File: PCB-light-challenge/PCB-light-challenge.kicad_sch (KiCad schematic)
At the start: 1 part

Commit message: Library toegevoegd
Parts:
- added U-PICO2: ~, symbol Light_challenge:Raspeberry_Pico
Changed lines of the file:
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@@
 (kicad_sch (version 20230121) (generator eeschema)
   (paper "A4")
+  (symbol (lib_id "Light_challenge:Raspeberry_Pico") (at 72.39 81.28 0) (unit 1)
+    (in_bom yes) (on_board yes) (dnp no) (fields_autoplaced)
+    (property "Reference" "U-PICO2" (at 87.63 79.0481 0)
+      (effects (font (size 1.27 1.27)))
+    )
+    (property "Value" "~" (at 72.39 81.28 0)
+      (effects (font (size 1.27 1.27)))
+    )
+    (property "Footprint" "" (at 72.39 81.28 0)
+      (effects (font (size 1.27 1.27)) hide)
+    )
+    (property "Datasheet" "" (at 72.39 81.28 0)
+      (effects (font (size 1.27 1.27)) hide)
+    )
+    (pin "")
+    (pin "")
+    (pin "")
+    (pin "")
+    (pin "")
+    (pin "")
+    (pin "")
+    (pin "")
+    (pin "")
+    (pin "")
+    (pin "")
+    (pin "")
+    (pin "")
+    (pin "")
+    (pin "")
+    (pin "")
+    (pin "")
+    (pin "")
+    (pin "")
+    (pin "")
+    (pin "")
+    (pin "")
+    (pin "")
+    (pin "")
+    (pin "")
+    (pin "")
+    (pin "")
+    (pin "")
+    (pin "")
+    (pin "")
+    (pin "")
+    (pin "")
+    (pin "")
+    (pin "")
+    (pin "")
+    (pin "")
+    (pin "")
+    (pin "")
+    (pin "")
+    (pin "")
+    (pin "")
+    (pin "")
+    (pin "")
+    (instances
+      (project "PCB-light-challenge"
+        (path "/35573e8f-7834-430c-81d2-239f316c7834"
+          (reference "U-PICO2") (unit 1)
+        )
+      )
+    )
+  )
   (symbol (lib_id "Light_challenge:Raspeberry_Pico") (at 127 81.28 0) (unit 1)
     (in_bom yes) (on_board yes) (dnp no) (fields_autoplaced)
-    (property "Reference" "U-PICO1" (at 142.24 77.47 0)
+    (property "Reference" "U-PICO1" (at 142.24 77.47 0) (show_name)
       (effects (font (size 1.27 1.27)))
     )
-    (property "Value" "~" (at 127 81.28 0)
+    (property "Value" "~" (at 127 81.28 0) (show_name)
       (effects (font (size 1.27 1.27)))
     )

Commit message: Opnieuw
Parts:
- removed U-PICO1: ~, symbol Light_challenge:Raspeberry_Pico
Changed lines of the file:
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@@
-    )
-  )
-  (symbol (lib_id "Light_challenge:Raspeberry_Pico") (at 127 81.28 0) (unit 1)
-    (in_bom yes) (on_board yes) (dnp no) (fields_autoplaced)
-    (property "Reference" "U-PICO1" (at 142.24 77.47 0) (show_name)
-      (effects (font (size 1.27 1.27)))
-    )
-    (property "Value" "~" (at 127 81.28 0) (show_name)
-      (effects (font (size 1.27 1.27)))
-    )
-    (property "Footprint" "" (at 127 81.28 0)
-      (effects (font (size 1.27 1.27)) hide)
-    )
-    (property "Datasheet" "" (at 127 81.28 0)
-      (effects (font (size 1.27 1.27)) hide)
-    )
-    (pin "")
-    (pin "")
-    (pin "")
-    (pin "")
-    (pin "")
-    (pin "")
-    (pin "")
-    (pin "")
-    (pin "")
-    (pin "")
-    (pin "")
-    (pin "")
-    (pin "")
-    (pin "")
-    (pin "")
-    (pin "")
-    (pin "")
-    (pin "")
-    (pin "")
-    (pin "")
-    (pin "")
-    (pin "")
-    (pin "")
-    (pin "")
-    (pin "")
-    (pin "")
-    (pin "")
-    (pin "")
-    (pin "")
-    (pin "")
-    (pin "")
-    (pin "")
-    (pin "")
-    (pin "")
-    (pin "")
-    (pin "")
-    (pin "")
-    (pin "")
-    (pin "")
-    (pin "")
-    (pin "")
-    (pin "")
-    (pin "")
-    (instances
-      (project "PCB-light-challenge"
-        (path "/35573e8f-7834-430c-81d2-239f316c7834"
-          (reference "U-PICO1") (unit 1)
-        )
-      )
     )
   )

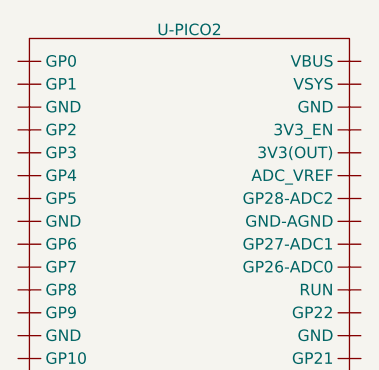
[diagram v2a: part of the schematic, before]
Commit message: pico footprint
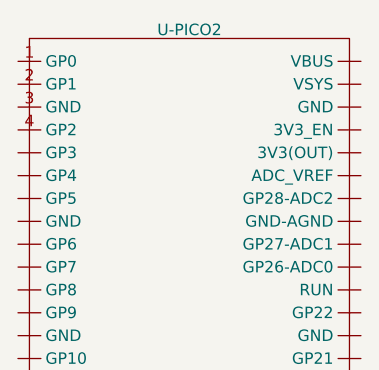
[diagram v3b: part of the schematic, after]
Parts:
- U-PICO2: footprint (none) -> custom_footprint_pico:Pico_light challenge
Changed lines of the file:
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@@
       (effects (font (size 1.27 1.27)))
     )
-    (property "Footprint" "" (at 72.39 81.28 0)
+    (property "Footprint" "custom_footprint_pico:Pico_light challenge" (at 72.39 81.28 0)
       (effects (font (size 1.27 1.27)) hide)
     )
@@
     (pin "")
     (pin "")
-    (pin "")
-    (pin "")
-    (pin "")
-    (pin "")
+    (pin "1")
+    (pin "2")
+    (pin "3")
+    (pin "4")
     (instances
       (project "PCB-light-challenge"

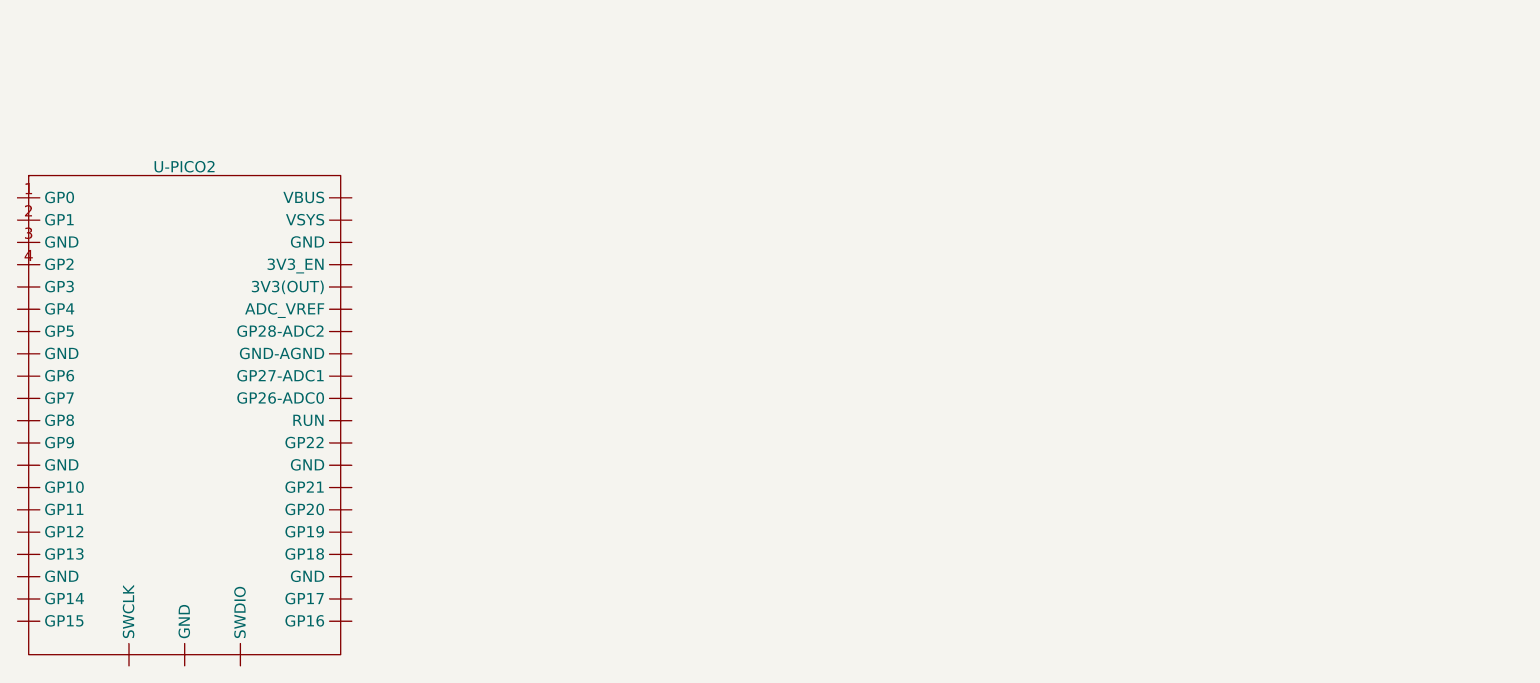
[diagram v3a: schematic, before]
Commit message: Hierarchische blad toegevoegd voor de microcontroller en battery charger
Dit moet gedaan worden voor elke deel van het totale circuit. Dit maakt de file beter leesbaar
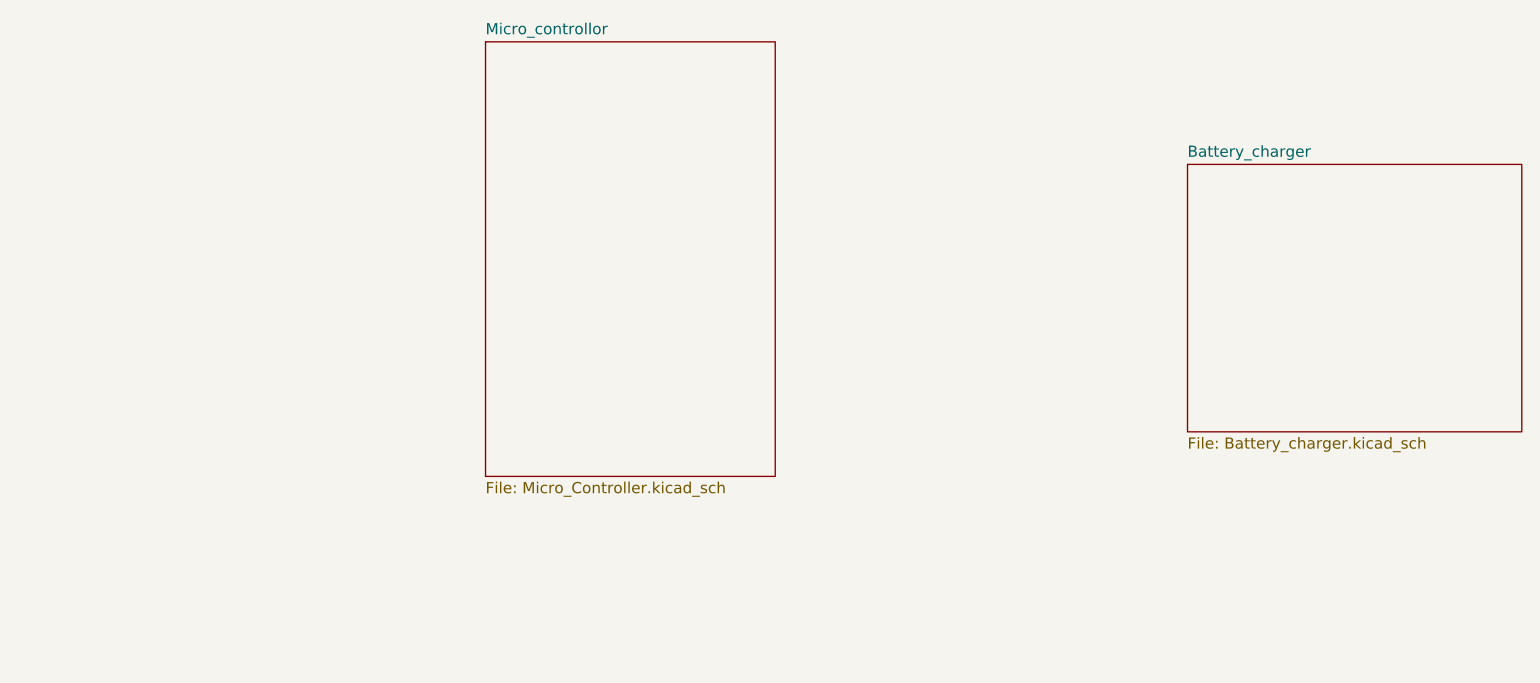
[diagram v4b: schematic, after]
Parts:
- removed U-PICO2: ~, custom_footprint_pico:Pico_light challenge, symbol Light_challenge:Raspeberry_Pico
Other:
- added sheet Battery_charger (Battery_charger.kicad_sch)
- added sheet Micro_controllor (Micro_Controller.kicad_sch)
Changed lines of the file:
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@@
 (kicad_sch (version 20230121) (generator eeschema)
   (paper "A4")
-  (symbol (lib_id "Light_challenge:Raspeberry_Pico") (at 72.39 81.28 0) (unit 1)
-    (in_bom yes) (on_board yes) (dnp no) (fields_autoplaced)
-    (property "Reference" "U-PICO2" (at 87.63 79.0481 0)
-      (effects (font (size 1.27 1.27)))
+  (sheet (at 201.93 78.74) (size 38.1 30.48) (fields_autoplaced)
+    (stroke (width 0.1524) (type solid))
+    (fill (color 0 0 0 0.0000))
+    (property "Sheetname" "Battery_charger" (at 201.93 78.0284 0)
+      (effects (font (size 1.27 1.27)) (justify left bottom))
     )
-    (property "Value" "~" (at 72.39 81.28 0)
-      (effects (font (size 1.27 1.27)))
+    (property "Sheetfile" "Battery_charger.kicad_sch" (at 201.93 109.8046 0)
+      (effects (font (size 1.27 1.27)) (justify left top))
     )
-    (property "Footprint" "custom_footprint_pico:Pico_light challenge" (at 72.39 81.28 0)
-      (effects (font (size 1.27 1.27)) hide)
-    )
-    (property "Datasheet" "" (at 72.39 81.28 0)
-      (effects (font (size 1.27 1.27)) hide)
-    )
-    (pin "")
-    (pin "")
-    (pin "")
-    (pin "")
-    (pin "")
-    (pin "")
-    (pin "")
-    (pin "")
-    (pin "")
-    (pin "")
-    (pin "")
-    (pin "")
-    (pin "")
-    (pin "")
-    (pin "")
-    (pin "")
-    (pin "")
-    (pin "")
-    (pin "")
-    (pin "")
-    (pin "")
-    (pin "")
-    (pin "")
-    (pin "")
-    (pin "")
-    (pin "")
-    (pin "")
-    (pin "")
-    (pin "")
-    (pin "")
-    (pin "")
-    (pin "")
-    (pin "")
-    (pin "")
-    (pin "")
-    (pin "")
-    (pin "")
-    (pin "")
-    (pin "")
-    (pin "1")
-    (pin "2")
-    (pin "3")
-    (pin "4")
     (instances
       (project "PCB-light-challenge"
-        (path "/35573e8f-7834-430c-81d2-239f316c7834"
-          (reference "U-PICO2") (unit 1)
-        )
+        (path "/35573e8f-7834-430c-81d2-239f316c7834" (page "2"))
       )
     )
+  )
+  (sheet (at 121.92 64.77) (size 33.02 49.53) (fields_autoplaced)
+    (stroke (width 0.1524) (type solid))
+    (fill (color 0 0 0 0.0000))
+    (property "Sheetname" "Micro_controllor" (at 121.92 64.0584 0)
+      (effects (font (size 1.27 1.27)) (justify left bottom))
+    )
+    (property "Sheetfile" "Micro_Controller.kicad_sch" (at 121.92 114.8846 0)
+      (effects (font (size 1.27 1.27)) (justify left top))
+    )
+    (instances
+      (project "PCB-light-challenge"
+        (path "/35573e8f-7834-430c-81d2-239f316c7834" (page "3"))
+      )
+    )

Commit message: Beetje meer bladen toegevoegd
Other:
- added sheet BMS (BMS.kicad_sch)
- added sheet Force_sensor (Force.kicad_sch)
- added sheet LEDS (LEDS.kicad_sch)
- added sheet Light_sensor (Light_sensor.kicad_sch)
- added sheet PIR_Sensor (PIR.kicad_sch)
- added sheet USB (USB.kicad_sch)
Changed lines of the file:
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@@
 (kicad_sch (version 20230121) (generator eeschema)
   (paper "A4")
-  (sheet (at 201.93 78.74) (size 38.1 30.48) (fields_autoplaced)
+  (sheet (at 38.1 25.4) (size 38.1 34.29) (fields_autoplaced)
     (stroke (width 0.1524) (type solid))
     (fill (color 0 0 0 0.0000))
-    (property "Sheetname" "Battery_charger" (at 201.93 78.0284 0)
+    (property "Sheetname" "LEDS" (at 38.1 24.6884 0)
       (effects (font (size 1.27 1.27)) (justify left bottom))
     )
-    (property "Sheetfile" "Battery_charger.kicad_sch" (at 201.93 109.8046 0)
+    (property "Sheetfile" "LEDS.kicad_sch" (at 38.1 60.2746 0)
+      (effects (font (size 1.27 1.27)) (justify left top))
+    )
+    (instances
+      (project "PCB-light-challenge"
+        (path "/35573e8f-7834-430c-81d2-239f316c7834" (page "6"))
+      )
+    )
+  )
+  (sheet (at 200.66 76.2) (size 38.1 30.48) (fields_autoplaced)
+    (stroke (width 0.1524) (type solid))
+    (fill (color 0 0 0 0.0000))
+    (property "Sheetname" "Battery_charger" (at 200.66 75.4884 0)
+      (effects (font (size 1.27 1.27)) (justify left bottom))
+    )
+    (property "Sheetfile" "Battery_charger.kicad_sch" (at 200.66 107.2646 0)
       (effects (font (size 1.27 1.27)) (justify left top))
     )
@@
       )
     )
+  )
+  (sheet (at 38.1 115.57) (size 40.64 21.59) (fields_autoplaced)
+    (stroke (width 0.1524) (type solid))
+    (fill (color 0 0 0 0.0000))
+    (property "Sheetname" "Light_sensor" (at 38.1 114.8584 0)
+      (effects (font (size 1.27 1.27)) (justify left bottom))
+    )
+    (property "Sheetfile" "Light_sensor.kicad_sch" (at 38.1 137.7446 0)
+      (effects (font (size 1.27 1.27)) (justify left top))
+    )
+    (instances
+      (project "PCB-light-challenge"
+        (path "/35573e8f-7834-430c-81d2-239f316c7834" (page "8"))
+      )
+    )
+  )
+  (sheet (at 200.66 115.57) (size 35.56 24.13) (fields_autoplaced)
+    (stroke (width 0.1524) (type solid))
+    (fill (color 0 0 0 0.0000))
+    (property "Sheetname" "USB" (at 200.66 114.8584 0)
+      (effects (font (size 1.27 1.27)) (justify left bottom))
+    )
+    (property "Sheetfile" "USB.kicad_sch" (at 200.66 140.2846 0)
+      (effects (font (size 1.27 1.27)) (justify left top))
+    )
+    (instances
+      (project "PCB-light-challenge"
+        (path "/35573e8f-7834-430c-81d2-239f316c7834" (page "5"))
+      )
+    )
+  )
+  (sheet (at 38.1 76.2) (size 39.37 26.67) (fields_autoplaced)
+    (stroke (width 0.1524) (type solid))
+    (fill (color 0 0 0 0.0000))
+    (property "Sheetname" "PIR_Sensor" (at 38.1 75.4884 0)
+      (effects (font (size 1.27 1.27)) (justify left bottom))
+    )
+    (property "Sheetfile" "PIR.kicad_sch" (at 38.1 103.4546 0)
+      (effects (font (size 1.27 1.27)) (justify left top))
+    )
+    (instances
+      (project "PCB-light-challenge"
+        (path "/35573e8f-7834-430c-81d2-239f316c7834" (page "7"))
+      )
+    )
+  )
+  (sheet (at 200.66 40.64) (size 36.83 27.94) (fields_autoplaced)
+    (stroke (width 0.1524) (type solid))
+    (fill (color 0 0 0 0.0000))
+    (property "Sheetname" "BMS" (at 200.66 39.9284 0)
+      (effects (font (size 1.27 1.27)) (justify left bottom))
+    )
+    (property "Sheetfile" "BMS.kicad_sch" (at 200.66 69.1646 0)
+      (effects (font (size 1.27 1.27)) (justify left top))
+    )
+    (instances
+      (project "PCB-light-challenge"
+        (path "/35573e8f-7834-430c-81d2-239f316c7834" (page "4"))
+      )
+    )
+  )
+  (sheet (at 38.1 146.05) (size 40.64 22.86) (fields_autoplaced)
+    (stroke (width 0.1524) (type solid))
+    (fill (color 0 0 0 0.0000))
+    (property "Sheetname" "Force_sensor" (at 38.1 145.3384 0)
+      (effects (font (size 1.27 1.27)) (justify left bottom))
+    )
+    (property "Sheetfile" "Force.kicad_sch" (at 38.1 169.4946 0)
+      (effects (font (size 1.27 1.27)) (justify left top))
+    )
+    (instances
+      (project "PCB-light-challenge"
+        (path "/35573e8f-7834-430c-81d2-239f316c7834" (page "9"))
+      )
+    )

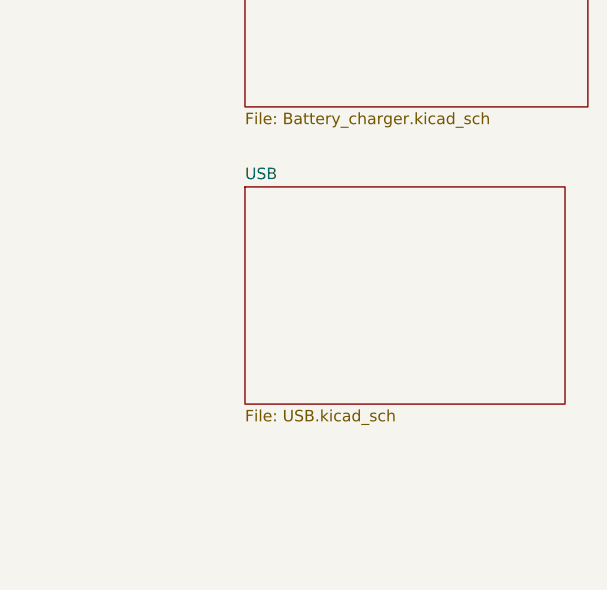
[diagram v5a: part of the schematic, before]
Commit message: USB blad weg gehaald plus BQ25895 toegevoegd
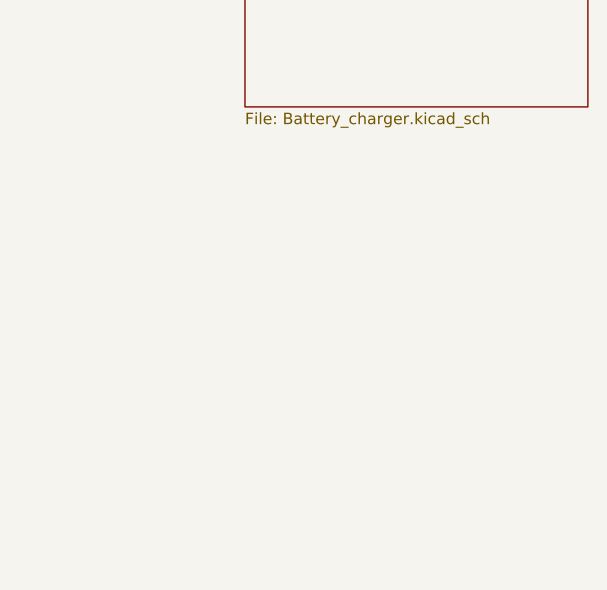
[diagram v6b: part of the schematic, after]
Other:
- removed sheet USB
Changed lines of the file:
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@@
-    )
-  )
-  (sheet (at 200.66 115.57) (size 35.56 24.13) (fields_autoplaced)
-    (stroke (width 0.1524) (type solid))
-    (fill (color 0 0 0 0.0000))
-    (property "Sheetname" "USB" (at 200.66 114.8584 0)
-      (effects (font (size 1.27 1.27)) (justify left bottom))
-    )
-    (property "Sheetfile" "USB.kicad_sch" (at 200.66 140.2846 0)
-      (effects (font (size 1.27 1.27)) (justify left top))
-    )
-    (instances
-      (project "PCB-light-challenge"
-        (path "/35573e8f-7834-430c-81d2-239f316c7834" (page "5"))
-      )
     )
   )

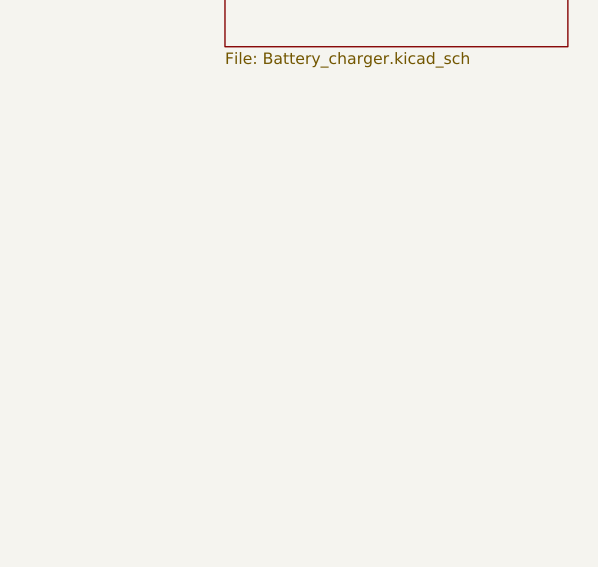
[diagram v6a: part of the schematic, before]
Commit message: Batterij charger foorprint en symbol toegevoegd, BMS schema getekend , LDO symbol en footprint toegevoegd
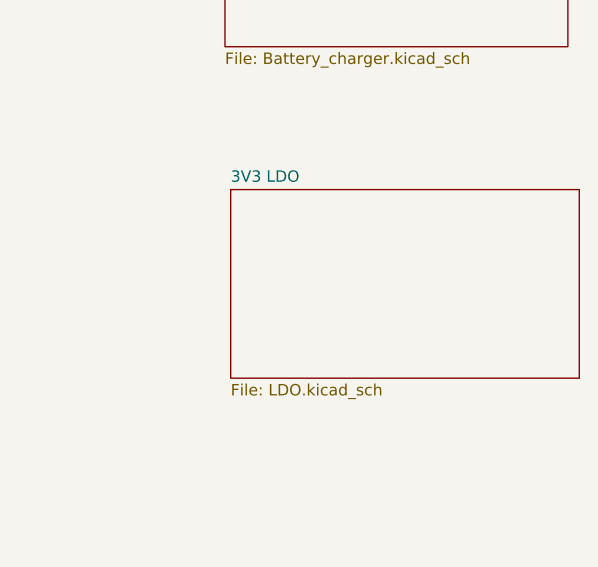
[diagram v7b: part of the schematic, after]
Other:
- added sheet 3V3 LDO (LDO.kicad_sch)
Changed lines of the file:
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@@
+    )
+  )
+  (sheet (at 201.295 122.555) (size 38.735 20.955) (fields_autoplaced)
+    (stroke (width 0.1524) (type solid))
+    (fill (color 0 0 0 0.0000))
+    (property "Sheetname" "3V3 LDO" (at 201.295 121.8434 0)
+      (effects (font (size 1.27 1.27)) (justify left bottom))
+    )
+    (property "Sheetfile" "LDO.kicad_sch" (at 201.295 144.0946 0)
+      (effects (font (size 1.27 1.27)) (justify left top))
+    )
+    (instances
+      (project "PCB-light-challenge"
+        (path "/35573e8f-7834-430c-81d2-239f316c7834" (page "9"))
+      )
     )
   )
